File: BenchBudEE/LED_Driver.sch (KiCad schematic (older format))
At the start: 0 parts

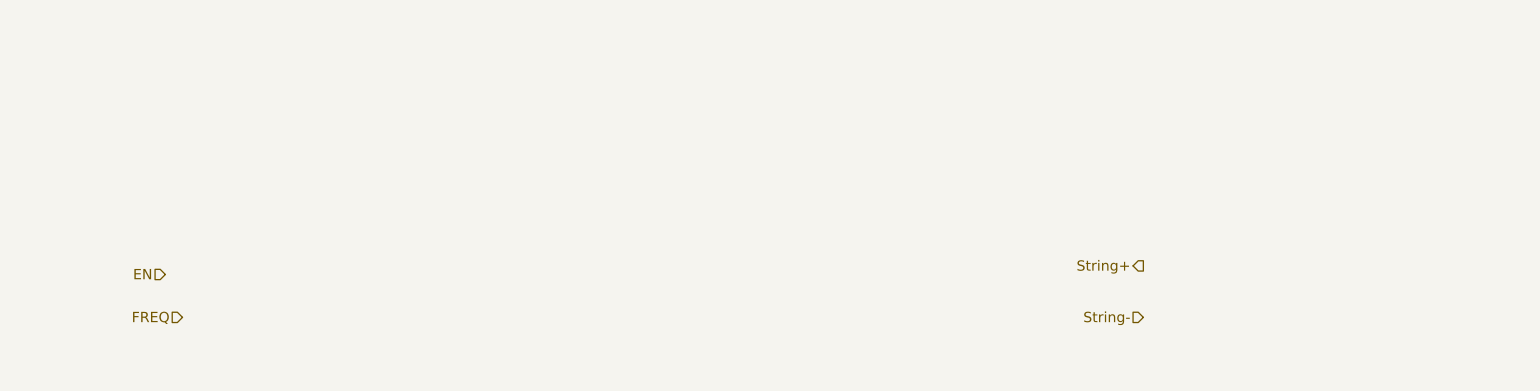
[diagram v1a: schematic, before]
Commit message: LED Driver block diagram
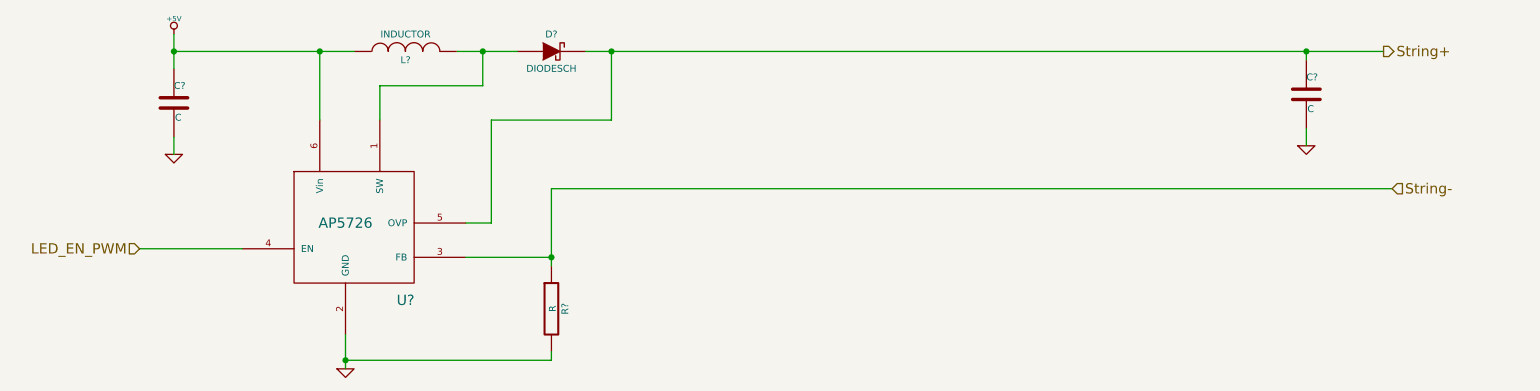
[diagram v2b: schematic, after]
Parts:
- added C? (x2): C, ~, symbol C
- added D?: DIODESCH, ~, symbol DIODESCH
- added L?: INDUCTOR, ~, symbol INDUCTOR
- added R?: R, ~, symbol R
- added U?: AP5726, symbol AP5726
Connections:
- net String+: now also C?.1, D?.2 (K), U?.5 (OVP)
- net String-: now also R?.1, U?.3 (FB)
- new net: D?.1 (A), L?.2, U?.1 (SW)
- new net +5V: C?.1, L?.1, U?.6 (Vin)
- new net GND: C?.2, C?.2, R?.2, U?.2 (GND)
- new net LED_EN_PWM: U?.4 (EN)
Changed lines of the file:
@@
 $Descr A4 11693 8268
 encoding utf-8
-Sheet 5 9
+Sheet 4 9
 Title ""
 Date "9 feb 2014"
@@
 Comment4 ""
 $EndDescr
-Text HLabel 2200 2450 0    60   Input ~ 0
-EN
-Text HLabel 2300 2700 0    60   Input ~ 0
-FREQ
-Text HLabel 7900 2400 0    60   Output ~ 0
+Text HLabel 2050 2300 0    60   Input ~ 0
+LED_EN_PWM
+Text HLabel 9300 1150 2    60   Output ~ 0
 String+
-Text HLabel 7900 2700 0    60   Input ~ 0
+Text HLabel 9350 1950 2    60   Input ~ 0
 String-
+$Comp
+L AP5726 U?
+U 1 1 52F7B15F
+P 3300 2150
+F 0 "U?" H 3600 1700 60  0000 C CNN
+F 1 "AP5726" H 3250 2150 60  0000 C CNN
+F 2 "" H 3200 2050 60  0000 C CNN
+F 3 "" H 3200 2050 60  0000 C CNN
+	1    3300 2150
+	1    0    0    -1
+$EndComp
+$Comp
+L +5V #PWR?
+U 1 1 52F7B180
+P 2250 1050
+F 0 "#PWR?" H 2250 1140 20  0001 C CNN
+F 1 "+5V" H 2250 1140 30  0000 C CNN
+F 2 "" H 2250 1050 60  0000 C CNN
+F 3 "" H 2250 1050 60  0000 C CNN
+	1    2250 1050
+	1    0    0    -1
+$EndComp
+$Comp
+L GND #PWR?
+U 1 1 52F7B18F
+P 2250 1750
+F 0 "#PWR?" H 2250 1750 30  0001 C CNN
+F 1 "GND" H 2250 1680 30  0001 C CNN
+F 2 "" H 2250 1750 60  0000 C CNN
+F 3 "" H 2250 1750 60  0000 C CNN
+	1    2250 1750
+	1    0    0    -1
+$EndComp
+$Comp
+L GND #PWR?
+U 1 1 52F7B19C
+P 3250 3000
+F 0 "#PWR?" H 3250 3000 30  0001 C CNN
+F 1 "GND" H 3250 2930 30  0001 C CNN
+F 2 "" H 3250 3000 60  0000 C CNN
+F 3 "" H 3250 3000 60  0000 C CNN
+	1    3250 3000
+	1    0    0    -1
+$EndComp
+$Comp
+L C C?
+U 1 1 52F7B1BA
+P 2250 1450
+F 0 "C?" H 2250 1550 40  0000 L CNN
+F 1 "C" H 2256 1365 40  0000 L CNN
+F 2 "~" H 2288 1300 30  0000 C CNN
+F 3 "~" H 2250 1450 60  0000 C CNN
+	1    2250 1450
+	1    0    0    -1
+$EndComp
+$Comp
+L INDUCTOR L?
+U 1 1 52F7B1DD
+P 3600 1150
+F 0 "L?" V 3550 1150 40  0000 C CNN
+F 1 "INDUCTOR" V 3700 1150 40  0000 C CNN
+F 2 "~" H 3600 1150 60  0000 C CNN
+F 3 "~" H 3600 1150 60  0000 C CNN
+	1    3600 1150
+	0    -1   -1   0
+$EndComp
+Wire Wire Line
+	2050 2300 2650 2300
+Wire Wire Line
+	3250 2800 3250 3000
+Wire Wire Line
+	2250 1050 2250 1250
+Wire Wire Line
+	2250 1650 2250 1750
+Wire Wire Line
+	2250 1150 3300 1150
+Wire Wire Line
+	3100 1150 3100 1550
+Connection ~ 2250 1150
+Connection ~ 3100 1150
+Wire Wire Line
+	3450 1550 3450 1350
+Wire Wire Line
+	3450 1350 4050 1350
+Wire Wire Line
+	4050 1350 4050 1150
+$Comp
+L C C?
+U 1 1 52F7B205
+P 8850 1400
+F 0 "C?" H 8850 1500 40  0000 L CNN
+F 1 "C" H 8856 1315 40  0000 L CNN
+F 2 "~" H 8888 1250 30  0000 C CNN
+F 3 "~" H 8850 1400 60  0000 C CNN
+	1    8850 1400
+	1    0    0    -1
+$EndComp
+Wire Wire Line
+	8850 1150 8850 1200
+Connection ~ 4050 1150
+$Comp
+L GND #PWR?
+U 1 1 52F7B218
+P 8850 1700
+F 0 "#PWR?" H 8850 1700 30  0001 C CNN
+F 1 "GND" H 8850 1630 30  0001 C CNN
+F 2 "" H 8850 1700 60  0000 C CNN
+F 3 "" H 8850 1700 60  0000 C CNN
+	1    8850 1700
+	1    0    0    -1
+$EndComp
+Wire Wire Line
+	8850 1600 8850 1700
+$Comp
+L DIODESCH D?
+U 1 1 52F7B254
+P 4450 1150
+F 0 "D?" H 4450 1250 40  0000 C CNN
+F 1 "DIODESCH" H 4450 1050 40  0000 C CNN
+F 2 "~" H 4450 1150 60  0000 C CNN
+F 3 "~" H 4450 1150 60  0000 C CNN
+	1    4450 1150
+	1    0    0    -1
+$EndComp
+Wire Wire Line
+	3900 1150 4250 1150
+Wire Wire Line
+	4650 1150 9300 1150
+Connection ~ 8850 1150
+Wire Wire Line
+	3950 2150 4100 2150
+Wire Wire Line
+	4100 2150 4100 1550
+Wire Wire Line
+	4100 1550 4800 1550
+Wire Wire Line
+	4800 1550 4800 1150
+Connection ~ 4800 1150
+$Comp
+L R R?
+U 1 1 52F7B2F0
+P 4450 2650
+F 0 "R?" V 4530 2650 40  0000 C CNN
+F 1 "R" V 4457 2651 40  0000 C CNN
+F 2 "~" V 4380 2650 30  0000 C CNN
+F 3 "~" H 4450 2650 30  0000 C CNN
+	1    4450 2650
+	1    0    0    -1
+$EndComp
+Wire Wire Line
+	3950 2350 4450 2350
+Wire Wire Line
+	4450 1950 4450 2400
+Wire Wire Line
+	4450 2900 4450 2950
+Wire Wire Line
+	4450 2950 3250 2950
+Connection ~ 3250 2950
+Wire Wire Line
+	9350 1950 4450 1950
+Connection ~ 4450 2350
 $EndSCHEMATC

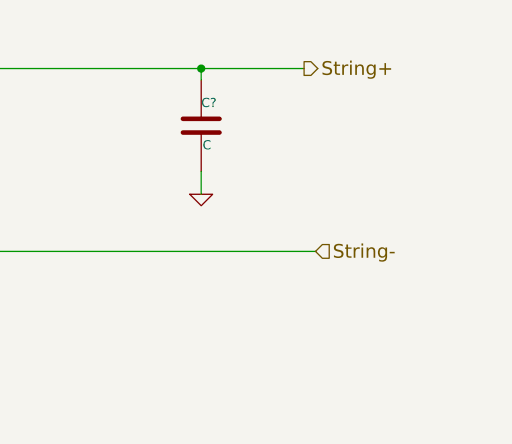
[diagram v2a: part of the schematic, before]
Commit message: Arduino block diagram
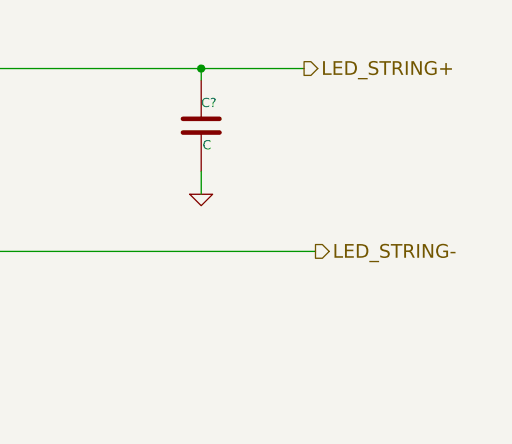
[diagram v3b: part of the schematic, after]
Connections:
- net String+ renamed LED_STRING+
- net String- renamed LED_STRING-
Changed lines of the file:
@@
 LED_EN_PWM
 Text HLabel 9300 1150 2    60   Output ~ 0
-String+
-Text HLabel 9350 1950 2    60   Input ~ 0
-String-
+LED_STRING+
+Text HLabel 9350 1950 2    60   Output ~ 0
+LED_STRING-
 $Comp
 L AP5726 U?

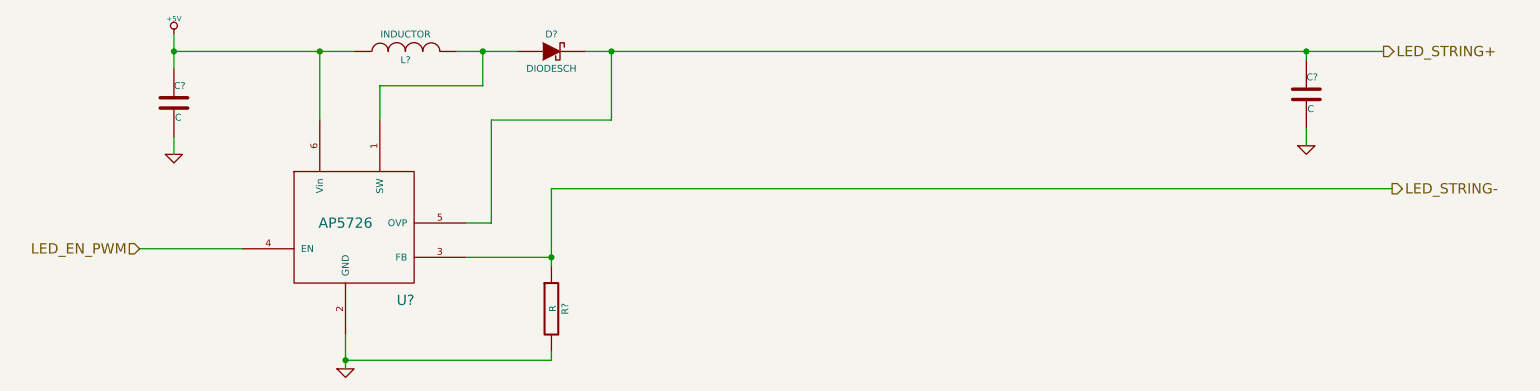
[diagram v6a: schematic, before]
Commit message: Associating and Placing the Relay Module
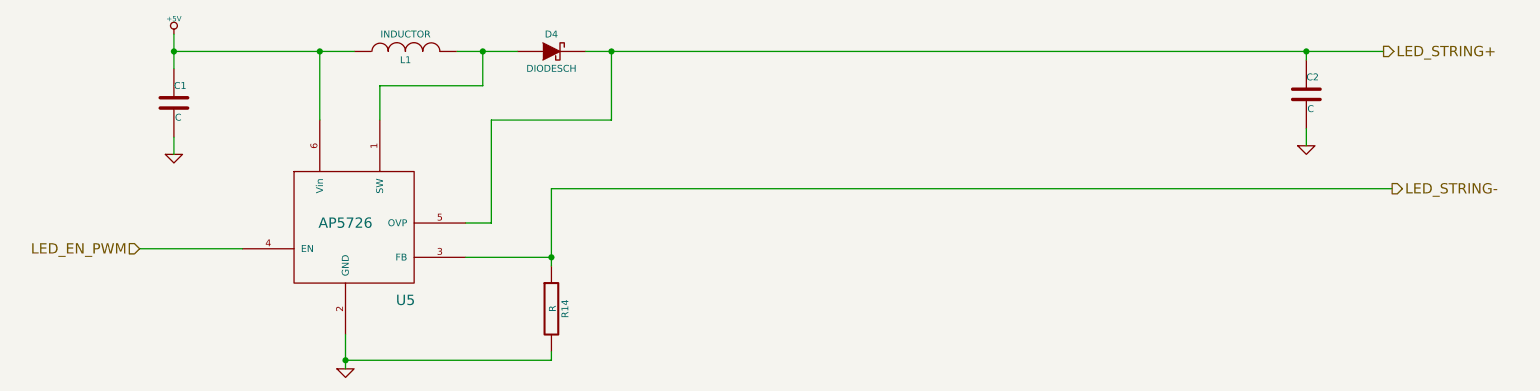
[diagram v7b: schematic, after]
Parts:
- gave numbers to parts that had none: 6
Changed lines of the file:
@@
 LED_STRING-
 $Comp
-L AP5726 U?
+L AP5726 U5
 U 1 1 52F7B15F
 P 3300 2150
-F 0 "U?" H 3600 1700 60  0000 C CNN
+F 0 "U5" H 3600 1700 60  0000 C CNN
 F 1 "AP5726" H 3250 2150 60  0000 C CNN
 F 2 "" H 3200 2050 60  0000 C CNN
@@
 $EndComp
 $Comp
-L +5V #PWR011
+L +5V #PWR11
 U 1 1 52F7B180
 P 2250 1050
-F 0 "#PWR011" H 2250 1140 20  0001 C CNN
+F 0 "#PWR11" H 2250 1140 20  0001 C CNN
 F 1 "+5V" H 2250 1140 30  0000 C CNN
 F 2 "" H 2250 1050 60  0000 C CNN
@@
 $EndComp
 $Comp
-L GND #PWR012
+L GND #PWR12
 U 1 1 52F7B18F
 P 2250 1750
-F 0 "#PWR012" H 2250 1750 30  0001 C CNN
+F 0 "#PWR12" H 2250 1750 30  0001 C CNN
 F 1 "GND" H 2250 1680 30  0001 C CNN
 F 2 "" H 2250 1750 60  0000 C CNN
@@
 $EndComp
 $Comp
-L GND #PWR013
+L GND #PWR13
 U 1 1 52F7B19C
 P 3250 3000
-F 0 "#PWR013" H 3250 3000 30  0001 C CNN
+F 0 "#PWR13" H 3250 3000 30  0001 C CNN
 F 1 "GND" H 3250 2930 30  0001 C CNN
 F 2 "" H 3250 3000 60  0000 C CNN
@@
 $EndComp
 $Comp
-L C C?
+L C C1
 U 1 1 52F7B1BA
 P 2250 1450
-F 0 "C?" H 2250 1550 40  0000 L CNN
+F 0 "C1" H 2250 1550 40  0000 L CNN
 F 1 "C" H 2256 1365 40  0000 L CNN
 F 2 "~" H 2288 1300 30  0000 C CNN
@@
 $EndComp
 $Comp
-L INDUCTOR L?
+L INDUCTOR L1
 U 1 1 52F7B1DD
 P 3600 1150
-F 0 "L?" V 3550 1150 40  0000 C CNN
+F 0 "L1" V 3550 1150 40  0000 C CNN
 F 1 "INDUCTOR" V 3700 1150 40  0000 C CNN
 F 2 "~" H 3600 1150 60  0000 C CNN
@@
 	4050 1350 4050 1150
 $Comp
-L C C?
+L C C2
 U 1 1 52F7B205
 P 8850 1400
-F 0 "C?" H 8850 1500 40  0000 L CNN
+F 0 "C2" H 8850 1500 40  0000 L CNN
 F 1 "C" H 8856 1315 40  0000 L CNN
 F 2 "~" H 8888 1250 30  0000 C CNN
@@
 Connection ~ 4050 1150
 $Comp
-L GND #PWR014
+L GND #PWR14
 U 1 1 52F7B218
 P 8850 1700
-F 0 "#PWR014" H 8850 1700 30  0001 C CNN
+F 0 "#PWR14" H 8850 1700 30  0001 C CNN
 F 1 "GND" H 8850 1630 30  0001 C CNN
 F 2 "" H 8850 1700 60  0000 C CNN
@@
 	8850 1600 8850 1700
 $Comp
-L DIODESCH D?
+L DIODESCH D4
 U 1 1 52F7B254
 P 4450 1150
-F 0 "D?" H 4450 1250 40  0000 C CNN
+F 0 "D4" H 4450 1250 40  0000 C CNN
 F 1 "DIODESCH" H 4450 1050 40  0000 C CNN
 F 2 "~" H 4450 1150 60  0000 C CNN
@@
 Connection ~ 4800 1150
 $Comp
-L R R?
+L R R14
 U 1 1 52F7B2F0
 P 4450 2650
-F 0 "R?" V 4530 2650 40  0000 C CNN
+F 0 "R14" V 4530 2650 40  0000 C CNN
 F 1 "R" V 4457 2651 40  0000 C CNN
 F 2 "~" V 4380 2650 30  0000 C CNN
